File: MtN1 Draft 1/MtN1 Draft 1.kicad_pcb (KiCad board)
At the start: 4 copper layers, 40 x 46 mm, 47 parts, among them J1 Screw_Terminal_01x02, J10 ServoPorts_2x3, J11 QWIIC, J2 Screw_Terminal_01x02, J3 Screw_Terminal_01x02, J4 Screw_Terminal_01x02, J5 Barrel_Jack, J6 VIN, J7 GND, J9 ServoPorts_2x3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

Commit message: Add files via upload
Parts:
- removed U8: SY8113BADC, Package_TO_SOT_SMD:SOT-23-6
- added C26: 10uF,25V, PCM_JLCPCB:C_0603, F.Cu at (186.0, 106.9)
- added C27: 100nF, PCM_JLCPCB:C_0603, F.Cu at (186.0, 109.1)
- added C28: 10pF, PCM_JLCPCB:C_0603, F.Cu at (186.0, 111.4)
- added C29: 10uF, PCM_JLCPCB:C_0603, F.Cu at (186.0, 113.6)
- added L3: 4.7uH, Inductor_SMD:L_1008_2520Metric, F.Cu at (182.3, 124.9)
- added R10: 68kΩ, PCM_JLCPCB:R_0603, F.Cu at (178.0, 118.1)
- added R12: 15kΩ, PCM_JLCPCB:R_0603, F.Cu at (178.0, 122.6)
- added SW1: 5.8 ZSPT, lcsc_footprints:C2681588_SW-TH_5_8ZSPT, F.Cu at (104.0, 104.2)
- added U6: SY8113BADC, lcsc_footprints:C78989_TSOT-23-6_L2_9-W1_6-P0_95-LS2_8-BR, F.Cu at (181.9, 116.9)
- J1, J2, J3, J4: footprint TerminalBlock_Phoenix:TerminalBlock_Phoenix_MKDS-1,5-2_1x02_P5.00mm_Horizontal -> lcsc_footprints:C8404_CONN-TH_WJ126V-5_0-2P
- U7: value ZSPT -> SY8113BADC; footprint Connector_PinHeader_2.54mm:PinHeader_2x03_P2.54mm_Vertical -> lcsc_footprints:C78989_TSOT-23-6_L2_9-W1_6-P0_95-LS2_8-BR
- moved Q1 116.9 mm to (102.9, 110.5), turned to 180 degrees
- moved D1 108.2 mm to (108.5, 110.0), turned to -90 degrees
- moved R1 105.8 mm to (110.5, 110.5), turned to 90 degrees
- moved U7 83.4 mm to (186.1, 116.9)
- moved D2 78.6 mm to (186.8, 120.6), turned to 0 degrees
- moved L2 61.2 mm to (182.3, 121.2)
- moved C20 49.3 mm to (182.1, 109.1)
- moved C21 49.3 mm to (182.1, 111.4)
- moved C22 49.3 mm to (182.1, 113.6)
- moved C12 47.8 mm to (178.3, 111.4)
- moved C13 47.8 mm to (178.3, 113.6)
- moved C7 47.8 mm to (178.3, 106.9)
- moved C8 47.8 mm to (178.3, 109.1)
- moved C1 46.3 mm to (174.4, 104.6)
- moved C2 46.3 mm to (174.4, 106.9)
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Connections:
- C13 pad 1: +3V3 -> GND
- C13 pad 2: GND -> +3V3
- C21 pad 1: Net-(U8-Pin_4) -> Net-(U6-BS)
- C21 pad 2: Net-(U8-Pin_2) -> Net-(U6-LX)
- C22 pad 1: +5V -> Net-(U6-FB)
- C22 pad 2: Net-(U8-Pin_1) -> +5V
- J11 pad 2: Net-(J11-Pin_2) -> unconnected-(J11-Pin_2-Pad2)
- J5 pad 1: Net-(U7-Pin_1) -> Net-(J5-Pad1)
- L2 pad 1: Net-(U8-Pin_4) -> Net-(U6-LX)
- R11 pad 1: GND -> Net-(U6-FB)
- R11 pad 2: Net-(U8-Pin_1) -> GND
- R3 pad 1: +3V3 -> SDA
- R3 pad 2: SCL -> +3V3
- R6 pad 1: +3V3 -> SCL
- R6 pad 2: SDA -> +3V3
- R9 pad 1: Net-(U8-Pin_1) -> +5V
- R9 pad 2: +5V -> Net-(U6-FB)
- U5 pad 25: GND -> +3V3
- U7 pad 1: Net-(U7-Pin_1) -> Net-(U7-BS)
- U7 pad 2: Net-(J11-Pin_2) -> GND
- U7 pad 3: Net-(Q1-D) -> Net-(U7-FB)
- U7 pad 4: +3V3 -> VCC
- U7 pad 5: unconnected-(U7-Pin_5-Pad5) -> VCC
- U7 pad 6: unconnected-(U7-Pin_6-Pad6) -> Net-(U7-LX)
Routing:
- net Net-(J5-Pad1): track 0.00 -> 17.2 mm
- net VCC: track 0.00 -> 8.07 mm, vias 0 -> 3
- net Net-(D1-A): track 0.00 -> 6.84 mm
- net Net-(Q1-D): track 0.00 -> 4.83 mm
- net GND: track 0.00 -> 4.78 mm, vias 0 -> 4
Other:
- board text added: "M1+"
- board text added: "M1-"
- board text added: "M2+"
- board text added: "M2-"
- board text added: "M3+"
- board text added: "M3-"
- board text added: "M4+"
- board text added: "M4-"
- board text added: "Qwiic"

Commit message: Updated project files up to Article 3
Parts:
- moved J6 14.5 mm to (114.4, 111.0)
- moved J7 14.5 mm to (117.5, 111.0)
- moved U4 11.1 mm to (126.5, 123.0)
- moved U2 10.5 mm to (126.0, 133.0)
- moved U1 9.66 mm to (126.0, 113.0)
- moved U5 6.03 mm to (116.0, 118.0)
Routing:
- net Net-(J5-Pad1): track 17.2 -> 0.00 mm
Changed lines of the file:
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@@
 				(font
 					(size 1.27 1.27)
+					(thickness 0.15)
 				)
 			)
@@
 				(font
 					(size 1.27 1.27)
+					(thickness 0.15)
 				)
 			)
@@
 	(footprint "Package_DFN_QFN:QFN-28-1EP_6x6mm_P0.65mm_EP4.25x4.25mm"
 		(layer "F.Cu")
-		(at 125.08 112 180)
+		(at 126.5 123 180)
 		(descr "QFN, 28 Pin (http://ww1.microchip.com/downloads/en/PackagingSpec/00000049BQ.pdf#page=289)")
 		(tags "QFN NoLead")
@@
 	(footprint "Package_SO:SSOP-24_5.3x8.2mm_P0.65mm"
 		(layer "F.Cu")
-		(at 135 127.5 90)
+		(at 126 133 90)
 		(descr "SSOP, 24 Pin (JEDEC MO-150 variation AG, 1.75mm body thickness, https://www.jedec.org/document_search?search_api_views_fulltext=MO-150, https://ww1.microchip.com/downloads/en/PackagingSpec/00000049BQ.pdf#page=398, https://www.analog.com/media/en/package-pcb-resources/package/pkg_pdf/ltc-legacy-ssop/ssop_24_05-08-1640.pdf)")
 		(tags "SSOP SO")
@@
 	(footprint "Package_DFN_QFN:QFN-28-1EP_6x6mm_P0.65mm_EP4.25x4.25mm"
 		(layer "F.Cu")
-		(at 116.58 112 180)
+		(at 116 118 180)
 		(descr "QFN, 28 Pin (http://ww1.microchip.com/downloads/en/PackagingSpec/00000049BQ.pdf#page=289)")
 		(tags "QFN NoLead")
@@
 	(footprint "Package_SO:SSOP-24_5.3x8.2mm_P0.65mm"
 		(layer "F.Cu")
-		(at 135 116.5 90)
+		(at 126 113 90)
 		(descr "SSOP, 24 Pin (JEDEC MO-150 variation AG, 1.75mm body thickness, https://www.jedec.org/document_search?search_api_views_fulltext=MO-150, https://ww1.microchip.com/downloads/en/PackagingSpec/00000049BQ.pdf#page=398, https://www.analog.com/media/en/package-pcb-resources/package/pkg_pdf/ltc-legacy-ssop/ssop_24_05-08-1640.pdf)")
 		(tags "SSOP SO")
@@
 	(footprint "TestPoint:TestPoint_Pad_2.0x2.0mm"
 		(layer "B.Cu")
-		(at 127 122)
+		(at 117.5 111)
 		(descr "SMD rectangular pad as test Point, square 2.0mm side length")
 		(tags "test point SMD pad rectangle square")
@@
 	(footprint "TestPoint:TestPoint_Pad_2.0x2.0mm"
 		(layer "B.Cu")
-		(at 123.91 122)
+		(at 114.41 111)
 		(descr "SMD rectangular pad as test Point, square 2.0mm side length")
 		(tags "test point SMD pad rectangle square")
@@
 	)
 	(segment
+		(start 110.17 111.65)
+		(end 110.5 111.32)
+		(width 1.2)
+		(layer "F.Cu")
+		(net "Net-(D1-A)")
+	)
+	(segment
+		(start 108.5 111.65)
+		(end 110.17 111.65)
+		(width 1.2)
+		(layer "F.Cu")
+		(net "Net-(D1-A)")
+	)
+	(segment
+		(start 103.875 111.45)
+		(end 108.3 111.45)
+		(width 1.2)
+		(layer "F.Cu")
+		(net "Net-(D1-A)")
+	)
+	(segment
+		(start 108.3 111.45)
+		(end 108.5 111.65)
+		(width 1.2)
+		(layer "F.Cu")
+		(net "Net-(D1-A)")
+	)
+	(segment
 		(start 119.7 126.5)
 		(end 120.5 126.5)
@@
 	)
 	(segment
-		(start 110.17 111.65)
-		(end 110.5 111.32)
-		(width 1.2)
-		(layer "F.Cu")
-		(net "Net-(D1-A)")
-	)
-	(segment
-		(start 108.5 111.65)
-		(end 110.17 111.65)
-		(width 1.2)
-		(layer "F.Cu")
-		(net "Net-(D1-A)")
-	)
-	(segment
-		(start 103.875 111.45)
-		(end 108.3 111.45)
-		(width 1.2)
-		(layer "F.Cu")
-		(net "Net-(D1-A)")
-	)
-	(segment
-		(start 108.3 111.45)
-		(end 108.5 111.65)
-		(width 1.2)
-		(layer "F.Cu")
-		(net "Net-(D1-A)")
-	)
-	(segment
-		(start 105 122.5)
-		(end 102 119.5)
-		(width 1.2)
-		(layer "B.Cu")
-		(net "Net-(J5-Pad1)")
-	)
-	(segment
-		(start 102 119.5)
-		(end 102 106.5)
-		(width 1.2)
-		(layer "B.Cu")
-		(net "Net-(J5-Pad1)")
-	)
-	(segment

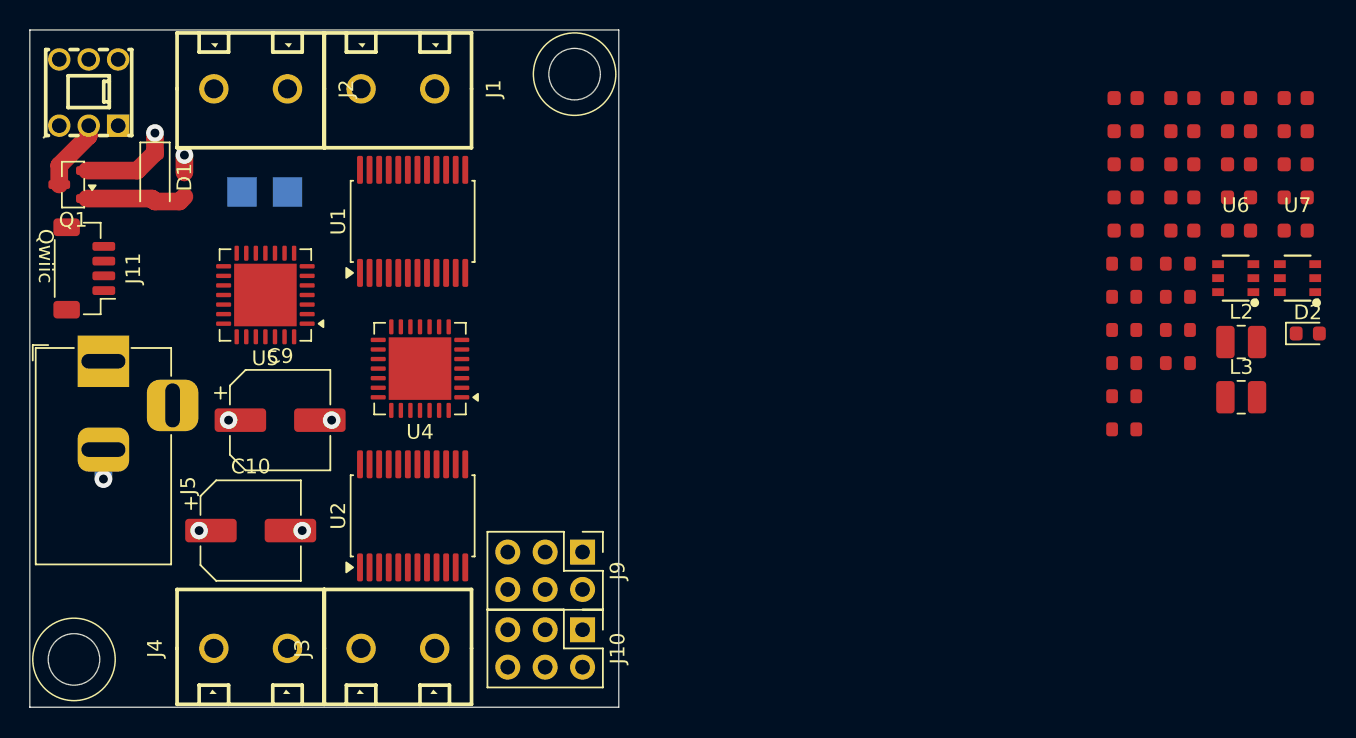
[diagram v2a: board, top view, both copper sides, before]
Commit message: Updated project files for Article 5
Article 5 isn't done yet, but just updating files for the future when it is done.
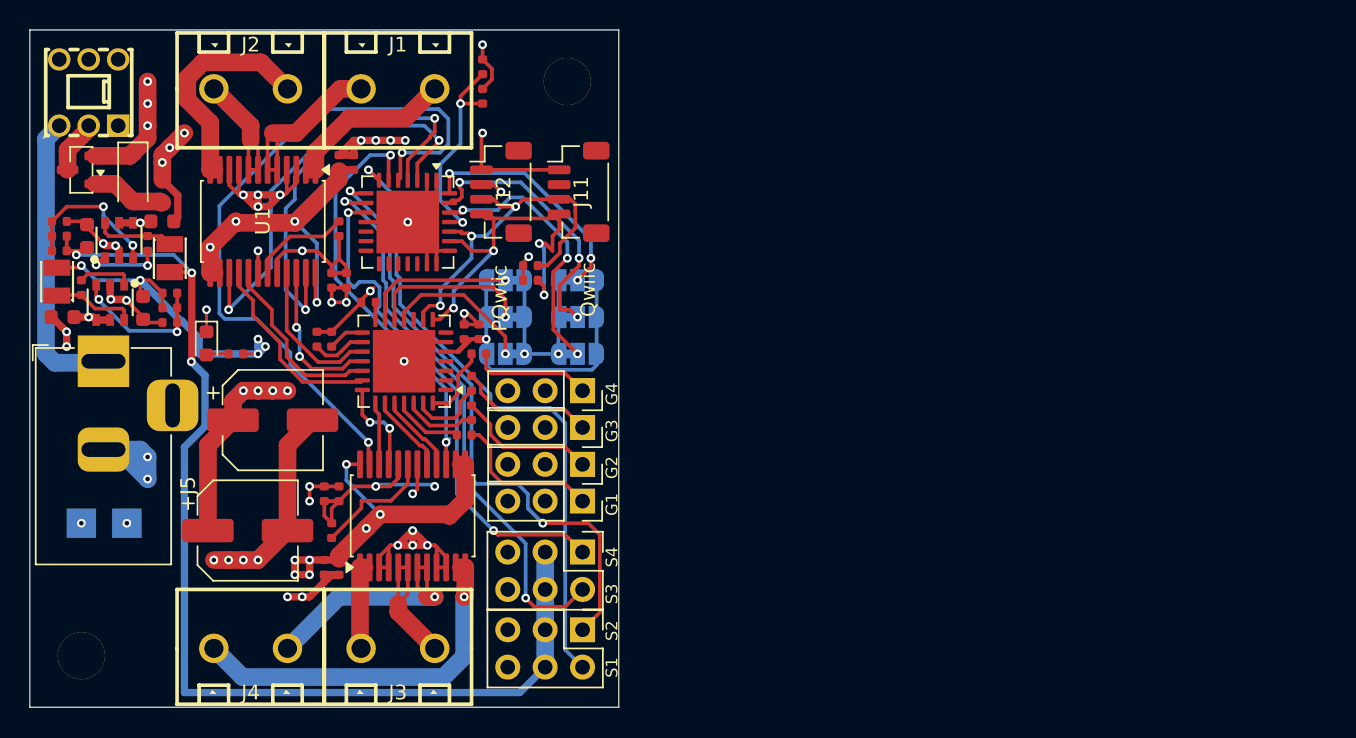
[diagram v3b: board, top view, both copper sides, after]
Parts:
- added J12: PQWIIC, Connector_JST:JST_SH_BM04B-SRSS-TB_1x04-1MP_P1.00mm_Vertical, F.Cu at (132.0, 111.0)
- added J13: GPIO_R1, Connector_PinSocket_2.54mm:PinSocket_1x03_P2.54mm_Vertical, F.Cu at (137.5, 129.5)
- added J14: GPIO_R2, Connector_PinSocket_2.54mm:PinSocket_1x03_P2.54mm_Vertical, F.Cu at (137.5, 127.0)
- added J15: GPIO_R3, Connector_PinSocket_2.54mm:PinSocket_1x03_P2.54mm_Vertical, F.Cu at (137.5, 124.5)
- added J8: GPIO_R0, Connector_PinSocket_2.54mm:PinSocket_1x03_P2.54mm_Vertical, F.Cu at (137.5, 132.0)
- added JP1: PAJP_1, Jumper:SolderJumper-3_P1.3mm_Bridged12_RoundedPad1.0x1.5mm, B.Cu at (137.2, 122.0)
- added JP2: PAJP_2, Jumper:SolderJumper-3_P1.3mm_Bridged12_RoundedPad1.0x1.5mm, B.Cu at (137.2, 119.5)
- added JP3: PAJP_3, Jumper:SolderJumper-3_P1.3mm_Bridged12_RoundedPad1.0x1.5mm, B.Cu at (137.2, 117.0)
- added JP4: MAJP_3, Jumper:SolderJumper-3_P1.3mm_Bridged12_RoundedPad1.0x1.5mm, B.Cu at (132.3, 117.0)
- added JP5: MAJP_2, Jumper:SolderJumper-3_P1.3mm_Bridged12_RoundedPad1.0x1.5mm, B.Cu at (132.3, 119.5)
- added JP6: MAJP_1, Jumper:SolderJumper-3_P1.3mm_Bridged12_RoundedPad1.0x1.5mm, B.Cu at (132.3, 122.0)
- added R13: 10kΩ, PCM_JLCPCB:R_0402, F.Cu at (120.5, 134.0)
- added R14: 330Ω, PCM_JLCPCB:R_0402, F.Cu at (130.5, 122.0)
- added R15: 330Ω, PCM_JLCPCB:R_0402, F.Cu at (130.0, 124.0)
- added R16: 330Ω, PCM_JLCPCB:R_0402, F.Cu at (130.0, 126.0)
- added R17: 330Ω, PCM_JLCPCB:R_0402, F.Cu at (129.5, 127.5)
- added R5: 10kΩ, PCM_JLCPCB:R_0402, F.Cu at (121.0, 113.5)
- added REF**: MountingHole_3.2mm_M3, MountingHole:MountingHole_3.2mm_M3, F.Cu at (103.5, 142.5)
- added REF**: MountingHole_3.2mm_M3, MountingHole:MountingHole_3.2mm_M3, F.Cu at (136.5, 103.5)
- C1, C12, C13, C14, C15, C2, C21, C22, C27, C28, C3, C4, C5, C6, C7, C8: footprint PCM_JLCPCB:C_0603 -> PCM_JLCPCB:C_0402
- J1: value Screw_Terminal_01x02 -> Motor_Port_1
- J2: value Screw_Terminal_01x02 -> Motor_Port_2
- J3: value Screw_Terminal_01x02 -> Motor_Port_3
- J4: value Screw_Terminal_01x02 -> Motor_Port_4
- L2, L3: footprint Inductor_SMD:L_1008_2520Metric -> lcsc_footprints:C98354_IND-SMD_L2_5-W2_0_WPN252012H
- R1: value 10k -> 10kΩ
- R10, R11, R12, R2, R3, R4, R6, R7, R8, R9: footprint PCM_JLCPCB:R_0603 -> PCM_JLCPCB:R_0402
- moved C26 84.7 mm to (102.2, 119.5)
- moved C27 82.9 mm to (103.5, 117.5), turned to -90 degrees
- moved C23 82.6 mm to (103.9, 114.0), turned to -90 degrees
- moved L3 80.8 mm to (101.9, 117.1), turned to 90 degrees
- moved U7 80.7 mm to (105.5, 118.5), turned to 90 degrees
- moved C22 80.1 mm to (102.0, 115.0)
- moved C29 78.5 mm to (107.7, 118.9), turned to 90 degrees
- moved C28 76.7 mm to (109.5, 117.9), turned to 180 degrees
- moved R11 76.3 mm to (102.0, 113.0)
- moved R9 76.0 mm to (102.0, 114.0), turned to 180 degrees
- moved U6 75.9 mm to (106.1, 114.3), turned to -90 degrees
- moved D2 74.8 mm to (112.0, 121.3), turned to -90 degrees
- moved C21 74.2 mm to (108.0, 114.5), turned to 90 degrees
- moved C20 73.2 mm to (109.0, 113.0), turned to 180 degrees
- moved L2 73.0 mm to (109.5, 115.5), turned to -90 degrees
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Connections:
- U1 pad 19: +3V3 -> Net-(U1-STBY)
- U2 pad 19: +3V3 -> Net-(U2-STBY)
- U4 pad 11: GND -> MA0
- U4 pad 12: GND -> MA1
- U4 pad 13: GND -> MA2
- U4 pad 25: unconnected-(U4-GPB0-Pad25) -> Net-(U4-GPB0)
- U4 pad 26: unconnected-(U4-GPB1-Pad26) -> Net-(U4-GPB1)
- U4 pad 27: unconnected-(U4-GPB2-Pad27) -> Net-(U4-GPB2)
- U4 pad 28: unconnected-(U4-GPB3-Pad28) -> Net-(U4-GPB3)
- U5 pad 26: GND -> PA0
- U5 pad 27: GND -> PA1
- U5 pad 28: GND -> PA2
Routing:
- net GND: track 4.78 -> 144.4 mm, vias 4 -> 44
- net +3V3: track 0.00 -> 95.8 mm, vias 0 -> 14
- net +5V: track 0.00 -> 75.6 mm, vias 0 -> 3
- net VCC: track 8.07 -> 73.2 mm, vias 3 -> 21
- net MD2 PWMA: track 0.00 -> 48.7 mm, vias 0 -> 2
- net SP1 PWM: track 0.00 -> 43.0 mm, vias 0 -> 1
- net SP2 PWM: track 0.00 -> 41.9 mm, vias 0 -> 2
- net SP3 PWM: track 0.00 -> 38.5 mm, vias 0 -> 2
- net SP4 PWM: track 0.00 -> 35.1 mm, vias 0 -> 2
- net MD1 PWMB: track 0.00 -> 29.9 mm, vias 0 -> 2
- net MD2 PWMB: track 0.00 -> 28.6 mm, vias 0 -> 2
- net MD1 PWMA: track 0.00 -> 27.6 mm, vias 0 -> 2
- net SCL: track 0.00 -> 26.3 mm, vias 0 -> 4
- net SDA: track 0.00 -> 25.5 mm, vias 0 -> 3
- net Net-(J4-Pin_1): track 0.00 -> 24.8 mm, vias 0 -> 1
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- added copper zone on In2.Cu, net +3V3
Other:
- outline, holes or cut-outs redrawn
- board text added: "G1"
- board text added: "G2"
- board text added: "G3"
- board text added: "G4"
- board text added: "GND"
- board text added: "PQwiic"
- board text added: "S1"
- board text added: "S2"
- board text added: "S3"
- board text added: "S4"
- board text added: "VIN"

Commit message: PCB layout cleanup
I'm going to get absolutely obliterated the second I show this off 💔
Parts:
- moved J3 10.0 mm to (115.0, 142.0)
- moved J4 10.0 mm to (125.0, 142.0)
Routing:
- net Net-(J4-Pin_1): track 24.8 -> 14.9 mm, vias 1 -> 0
- net Net-(J4-Pin_2): track 16.9 -> 8.61 mm, vias 1 -> 0
- net Net-(J3-Pin_1): track 5.83 -> 13.1 mm
- net Net-(J3-Pin_2): track 9.92 -> 14.6 mm
- net SCL: track 26.3 -> 25.3 mm
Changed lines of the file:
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@@
 	(footprint "lcsc_footprints:C8404_CONN-TH_WJ126V-5_0-2P"
 		(layer "F.Cu")
-		(at 125 142 90)
+		(at 115 142 90)
 		(descr "WJ126V-5.0-2P")
 		(property "Reference" "J3"
@@
 	(footprint "lcsc_footprints:C8404_CONN-TH_WJ126V-5_0-2P"
 		(layer "F.Cu")
-		(at 115 142 90)
+		(at 125 142 90)
 		(descr "WJ126V-5.0-2P")
 		(property "Reference" "J4"
@@
 		)
 	)
-	(gr_text "M4+"
+	(gr_text "M3+"
 		(at 111 144.5 180)
 		(layer "B.SilkS")
@@
 		)
 	)
-	(gr_text "M4-"
+	(gr_text "M3-"
 		(at 116 144.5 180)
 		(layer "B.SilkS")
@@
 		)
 	)
-	(gr_text "M3+"
+	(gr_text "M4+"
 		(at 121 144.5 180)
 		(layer "B.SilkS")
@@
 		)
 	)
-	(gr_text "M3-"
+	(gr_text "M4-"
 		(at 126 144.5 180)
 		(layer "B.SilkS")
@@
 	)
 	(segment
-		(start 110.136 118)
-		(end 110.008 117.872)
-		(width 0.25)
-		(layer "F.Cu")
-		(net "Net-(U7-FB)")
-	)
-	(segment
 		(start 110 120.5)
 		(end 110 119.88)
@@
 	)
 	(segment
-		(start 135 114.5)
-		(end 135.5 115)
-		(width 0.25)
-		(layer "F.Cu")
-		(net "SCL")
-	)
-	(segment
 		(start 135.65 112.8)
 		(end 135.95 112.5)
@@
 	)
 	(segment
-		(start 135.5 114)
-		(end 135.95 113.55)
+		(start 134.6 114.5)
+		(end 135 114.5)
 		(width 0.25)
 		(layer "F.Cu")
@@
 	)
 	(segment
-		(start 135.5 115)
-		(end 135.5 114)
-		(width 0.25)
-		(layer "F.Cu")
-		(net "SCL")
-	)
-	(segment
 		(start 128.607772 118.892228)
 		(end 128.784456 118.892228)
@@
 	)
 	(segment
-		(start 131.5 112.799999)
-		(end 135.65 112.8)
+		(start 135 114.5)
+		(end 135.95 113.55)
 		(width 0.25)
 		(layer "F.Cu")
@@
 	)
 	(segment
-		(start 134.6 114.5)
-		(end 135 114.5)
+		(start 131.5 112.799999)
+		(end 135.65 112.8)
 		(width 0.25)
 		(layer "F.Cu")
@@
 	(segment
 		(start 122.425 136.5)
-		(end 122.425 141.925)
+		(end 122.425 137.449999)
 		(width 1.2)
 		(layer "F.Cu")
@@
 	)
 	(segment
-		(start 122.425 136.5)
-		(end 122.725 136.5)
+		(start 122.425 137.449999)
+		(end 119.674999 140.2)
 		(width 1.2)
 		(layer "F.Cu")
@@
 	)
 	(segment
-		(start 122.425 141.925)
-		(end 122.5 142)
+		(start 119.674999 140.2)
+		(end 114.3 140.2)
+		(width 1.2)
+		(layer "F.Cu")
+		(net "Net-(J3-Pin_1)")
+	)
+	(segment
+		(start 114.3 140.2)
+		(end 112.5 142)
+		(width 1.2)
+		(layer "F.Cu")
+		(net "Net-(J3-Pin_1)")
+	)
+	(segment
+		(start 122.425 136.5)
+		(end 122.725 136.5)
 		(width 1.2)
 		(layer "F.Cu")
@@
 	)
 	(segment
-		(start 125.025 139.525)
-		(end 125.025 138.975)
+		(start 117.5 142)
+		(end 119.954415 142)
+		(width 1.2)
+		(layer "F.Cu")
+		(net "Net-(J3-Pin_2)")
+	)
+	(segment
+		(start 119.954415 142)
+		(end 122.979415 138.975)
 		(width 1.2)
 		(layer "F.Cu")
@@
 	)
 	(segment
-		(start 127.5 142)
-		(end 125.025 139.525)
+		(start 122.979415 138.975)
+		(end 125.025 138.975)
 		(width 1.2)
 		(layer "F.Cu")
@@
 	)
 	(segment
-		(start 127.5 138.5)
-		(end 127 138.5)
+		(start 127.5 142)
+		(end 127.5 139)
 		(width 1.2)
 		(layer "F.Cu")
@@
 	)
 	(segment
-		(start 127 138.5)
-		(end 126.975 138.475)
-		(width 1.2)
-		(layer "F.Cu")
-		(net "Net-(J4-Pin_2)")
-	)
-	(segment
 		(start 126.325 137.825)
 		(end 126.975 138.475)
@@
 		(net "Net-(J4-Pin_2)")
 	)
-	(via
-		(at 127.5 138.5)
-		(size 0.6)
-		(drill 0.3)
-		(layers "F.Cu" "B.Cu")
-		(net "Net-(J4-Pin_2)")
-	)
-	(segment
-		(start 121 138.5)
-		(end 127.5 138.5)
-		(width 1.2)
-		(layer "B.Cu")
-		(net "Net-(J4-Pin_2)")
-	)
 	(segment
-		(start 117.5 142)
-		(end 121 138.5)
+		(start 127.5 139)
+		(end 126.975 138.475)
 		(width 1.2)
-		(layer "B.Cu")
+		(layer "F.Cu")
 		(net "Net-(J4-Pin_2)")
 	)
@@
 	)
 	(segment
-		(start 129.575 136.5)
-		(end 129.575 138.425)
+		(start 129.575 142.470585)
+		(end 128.045585 144)
 		(width 1.2)
 		(layer "F.Cu")
@@
 	)
 	(segment
-		(start 129.575 138.425)
-		(end 129.5 138.5)
+		(start 128.045585 144)
+		(end 124.5 144)
 		(width 1.2)
 		(layer "F.Cu")
 		(net "Net-(J4-Pin_1)")
 	)
-	(via
-		(at 129.5 138.5)
-		(size 0.6)
-		(drill 0.3)
-		(layers "F.Cu" "B.Cu")
-		(net "Net-(J4-Pin_1)")
-	)
 	(segment
-		(start 129.5 142.545585)
-		(end 128.095585 143.95)
-		(width 1.2)
-		(layer "B.Cu")
-		(net "Net-(J4-Pin_1)")
-	)
-	(segment
-		(start 128.095585 143.95)
-		(end 114.45 143.95)
+		(start 124.5 144)
+		(end 122.5 142)
 		(width 1.2)
-		(layer "B.Cu")
+		(layer "F.Cu")
 		(net "Net-(J4-Pin_1)")
 	)
 	(segment
-		(start 114.45 143.95)
-		(end 112.5 142)
+		(start 122.425 141.925)
+		(end 122.5 142)
 		(width 1.2)
-		(layer "B.Cu")
+		(layer "F.Cu")
 		(net "Net-(J4-Pin_1)")
 	)
 	(segment
-		(start 129.5 138.5)
-		(end 129.5 142.545585)
+		(start 129.575 136.5)
+		(end 129.575 142.470585)
 		(width 1.2)
-		(layer "B.Cu")
+		(layer "F.Cu")
 		(net "Net-(J4-Pin_1)")
 	)
